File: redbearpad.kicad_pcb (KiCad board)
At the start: 2 copper layers, 96 x 64 mm, 15 parts, among them J1 PinSocket_1x14_P2.54mm_Vertic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, J2 PinSocket_1x14_P2.54mm_Vertic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, J3 PinSocket_1x04_P2.54mm_Vertic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, SW1 SW_Redragon_LowProfile_PCB_1.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, SW2 SW_Redragon_LowProfile_PCB_1.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, SW3 SW_Redragon_LowProfile_PCB_1.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, SW4 SW_Redragon_LowProfile_PCB_1.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, SW5 SW_Redragon_LowProfile_PCB_1.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, SW6 SW_Redragon_LowProfile_PCB_1.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, SW7 SW_Redragon_LowProfile_PCB_1.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, SW8 SW_Redragon_LowProfile_PCB_1.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

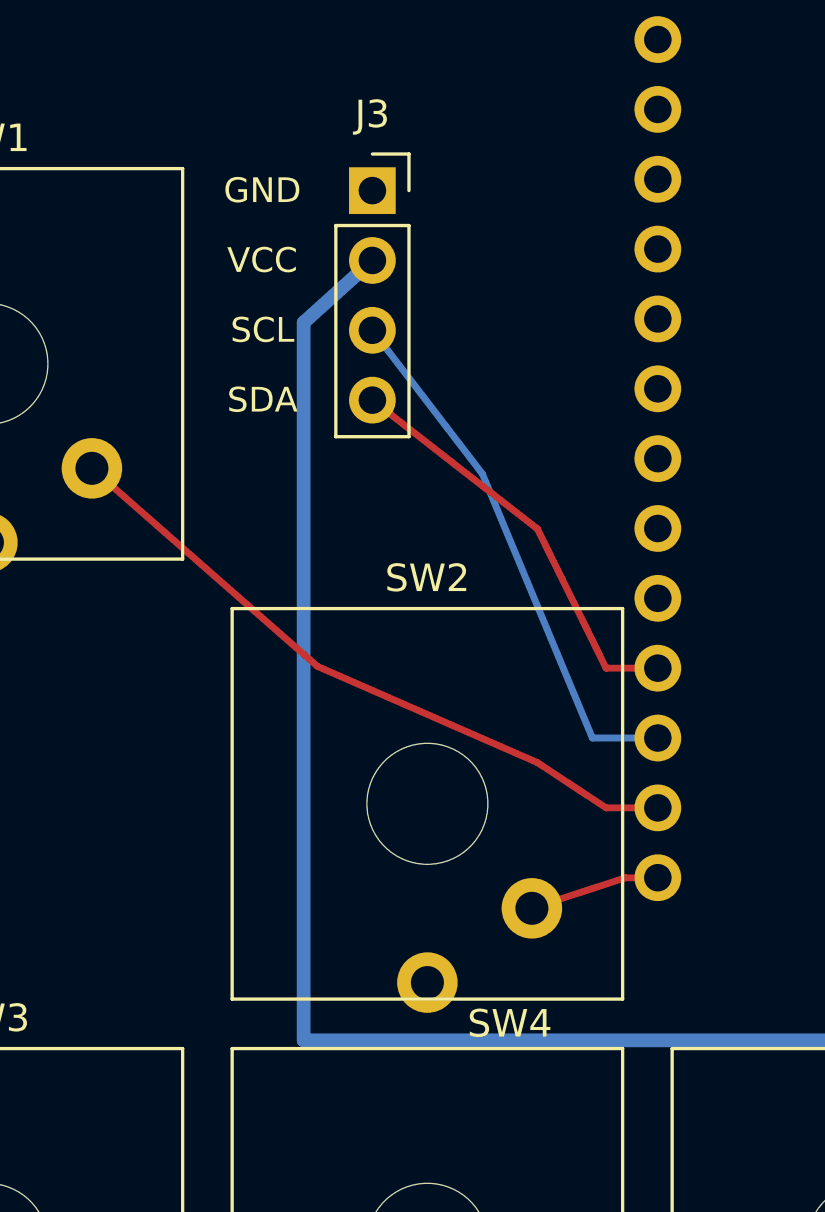
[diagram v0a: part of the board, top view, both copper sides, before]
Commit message: Corregir orden de pines OLED a SDA/SCL/VCC/GND segun ajuste fisico del modulo
- J3 reordenado en gen_sch.py y verify_netlist.py
- Reruteo de SDA/SCL/+3V3 a las nuevas posiciones de pad; SCL despeja el pad +3V3
- Serigrafia OLED invertida; renders y gerbers regenerados; spec actualizado
- DRC 0 violaciones / 0 unconnected, ERC 0, netlist OK

Co-Authored-By: Claude Fable 5 <noreply@anthropic.com>
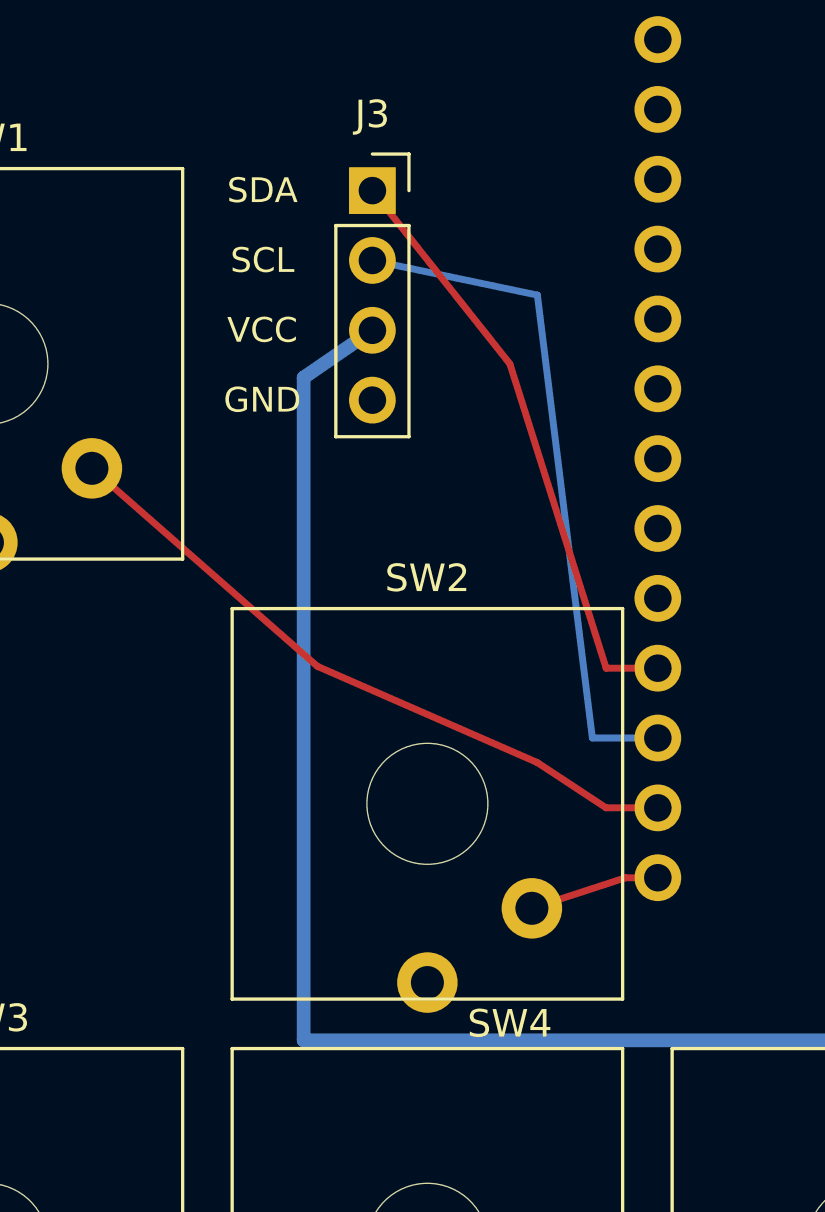
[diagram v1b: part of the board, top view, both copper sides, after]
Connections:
- J3 pad 1: GND -> SDA
- J3 pad 2: +3V3 -> SCL
- J3 pad 3: SCL -> +3V3
- J3 pad 4: SDA -> GND
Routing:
- net SDA: track 15.1 -> 21.5 mm
- net SCL: track 19.4 -> 24.7 mm
- net +3V3: track 99.7 -> 97.4 mm
